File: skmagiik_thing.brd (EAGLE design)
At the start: 160 x 100 mm, 24 parts, among them J1 MAGJACK-NOLABELS, U1 AUDIO-JACK, U2 AUDIO-JACK, U3 MAX3232

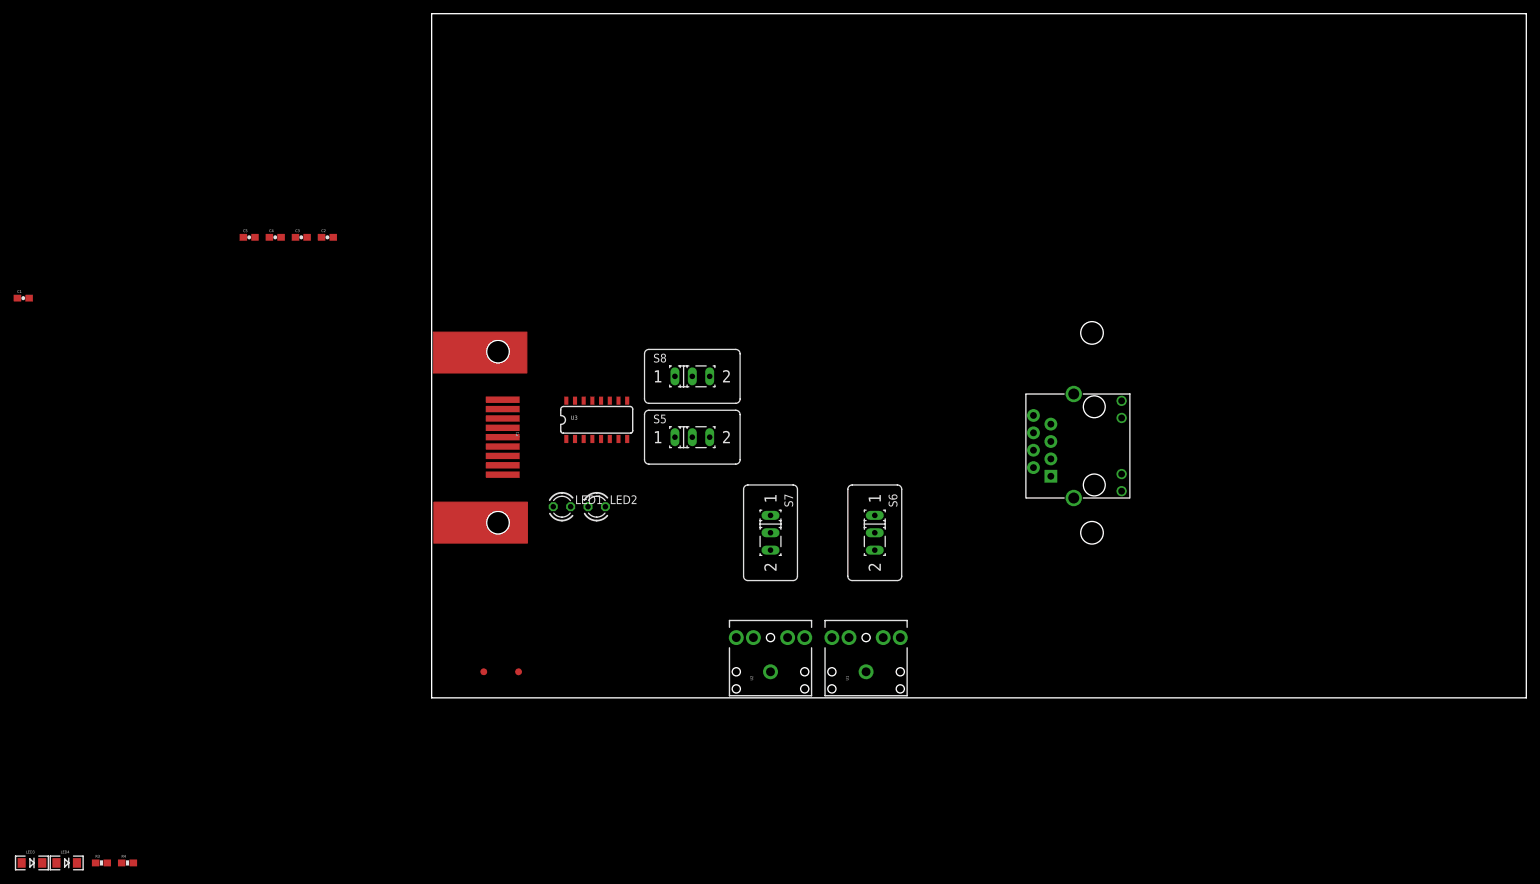
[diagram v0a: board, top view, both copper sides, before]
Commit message: changed to use modules, added pdf of layout
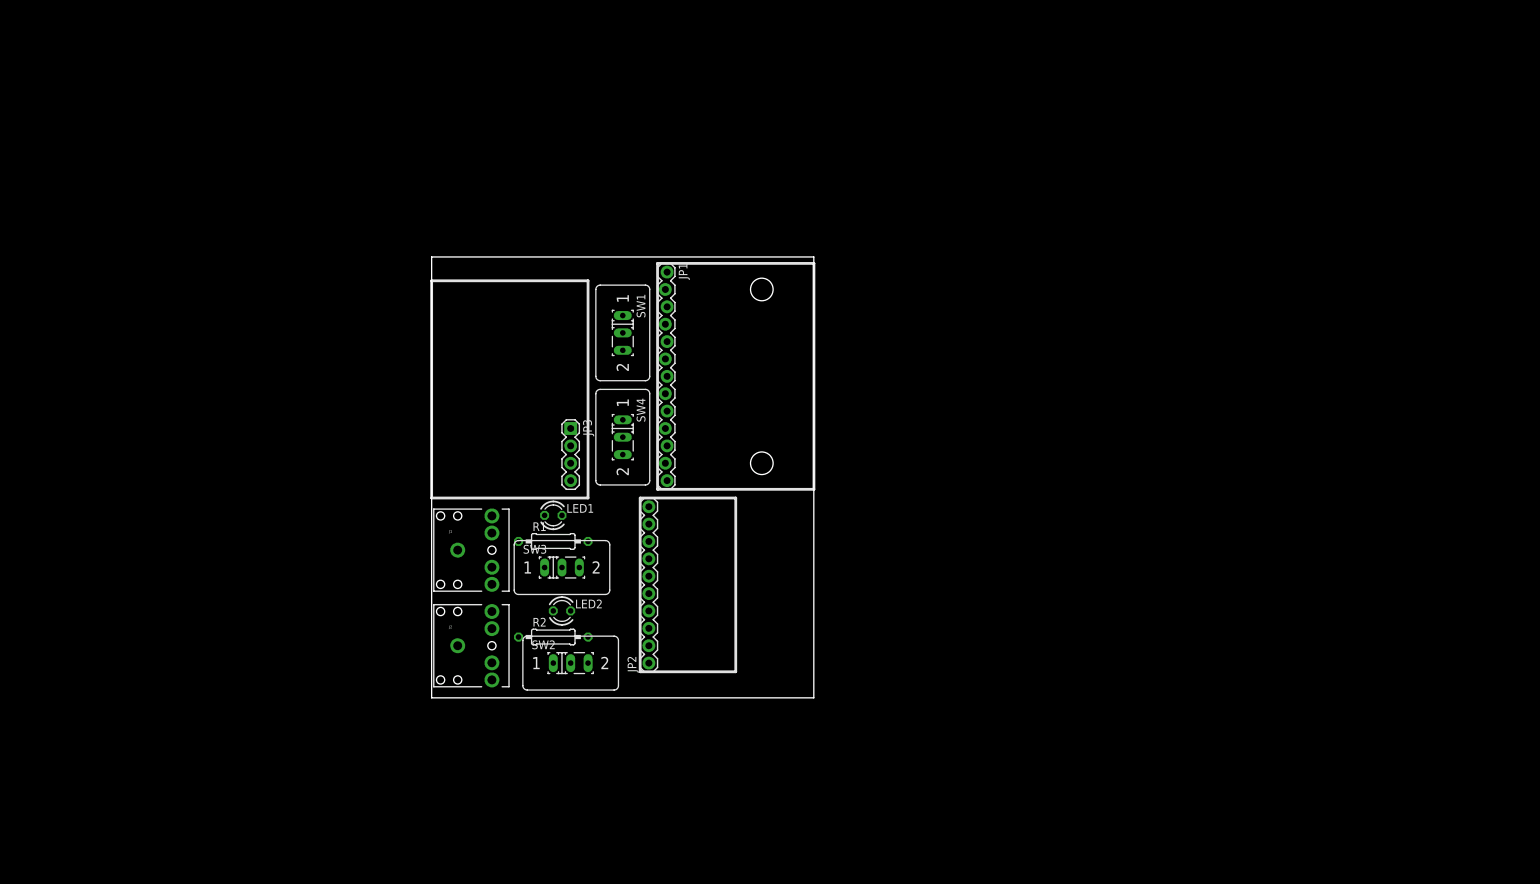
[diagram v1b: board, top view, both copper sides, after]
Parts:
- removed C1, C2, C3, C4, C5: .1uF, SparkFun-Capacitors:0603-CAP
- removed FID1, FID2: FIDUCIAL1X2, SparkFun-Aesthetics:FIDUCIAL-1X2
- removed LED3: Red, SparkFun:LED-1206
- removed LED4: Grn, SparkFun:LED-1206
- removed R3, R4: 330, SparkFun:0603-RES
- removed S5, S6, S7, S8: (no value), switch:M251
- removed U1, U2: AUDIO-JACK, SparkFun:AUDIO-JACK
- removed U3: MAX3232, SparkFun-DigitalIC:SO016
- added J2: AUDIO-JACK, SparkFun:AUDIO-JACK
- added JP2: M10", SparkFun-Connectors:1X10
- added JP3: (no value), SparkFun:1X04
- added R1, R2: (no value), resistor:0207/10
- added SW1, SW2, SW3, SW4: (no value), switch:M251
- J1: value MAGJACK-NOLABELS -> AUDIO-JACK; device SparkFun-Connectors:MAGJACK -> SparkFun:AUDIO-JACK
- JP1: value DB9 -> M13LOCK; device Testing:DB9-L17SM209S114T -> SparkFun-Connectors:1X13_LOCK
- moved J1 104.4 mm to (3.81, 21.6), turned to 0 degrees
- moved STANDOFF3 49.3 mm to (48.3, 34.3)
- moved STANDOFF5 48.7 mm to (48.3, 59.7)
- moved JP1 36.9 mm to (34.3, 62.2), turned to 270 degrees
- moved LED2 16.1 mm to (19.1, 12.7)
- moved LED1 1.80 mm to (17.8, 26.7)
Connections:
- removed net C1+: C1.1, U3.1
- removed net C1-: C1.2, U3.3
- removed net C2+: C2.1, U3.4
- removed net C2-: C2.2, U3.5
- removed net N$15: S8.3, U3.8
- removed net N$16: S7.3, U3.7
- removed net V+: C3.1, U3.2
- removed net V-: C4.1, U3.6
- net GND: now also J1.SLEEVE, J2.SLEEVE, JP1.9, JP2.6, JP3.2; no longer C3.2, C4.2, C5.2, J1.5, JP1.5, U1.SLEEVE, U2.SLEEVE, U3.15
- net N$1: now also J2.RING, R2.1; no longer LED2.K, U2.RING
- net N$10: now also JP2.1, SW2.3; no longer LED4.A, R4.1
- net N$11: now also JP2.9, JP3.4, SW1.1; no longer JP1.3, U3.13
- net N$12: now also LED1.K, R1.2; no longer JP1.2, U3.14
- net N$13: now also JP2.3, SW1.3; no longer LED4.C, S8.1, U3.11, U3.9
- net N$14: now also LED2.K, R2.2; no longer LED3.C, S7.1, U3.10, U3.12
- net N$17: now also JP1.12, SW1.2; no longer J1.2, S8.2
- net N$18: now also JP1.11, SW2.2; no longer J1.3, S7.2
- net N$2: now also J1.RING, R1.1; no longer LED1.K, U1.RING
- net N$3: now also JP1.7, SW4.1; no longer J1.7, S6.1
- net N$4: now also JP1.8, SW4.3; no longer J1.6, S6.3
- net N$5: now also JP1.10, SW3.3; no longer J1.4, S5.3
- net N$6: now also JP1.13, SW3.1; no longer J1.1, S5.1
- net N$7: now also SW4.2; no longer S6.2
- net N$8: now also SW3.2; no longer S5.2
- net N$9: now also JP2.7, JP3.3, SW2.1; no longer LED3.A, R3.1
- net VCC: now also J1.TIP, J2.TIP, JP1.6, JP2.5, JP3.1; no longer C5.1, J1.8, R3.2, R4.2, U1.TIP, U2.TIP, U3.16
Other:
- board size 160 x 100 mm -> 55.9 x 64.4 mm

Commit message: modifyed layout
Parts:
- moved SW4 34.2 mm to (19.1, 5.08), turned to 0 degrees
- moved SW2 33.9 mm to (27.9, 38.1), turned to 270 degrees
- moved JP2 32.2 mm to (36.8, 36.8)
- moved STANDOFF3 30.5 mm to (48.3, 3.81)
- moved JP1 30.5 mm to (34.3, 31.8)
- moved STANDOFF5 30.5 mm to (48.3, 29.2)
- moved R1 10.2 mm to (27.9, 21.6), turned to 270 degrees
- moved R2 10.2 mm to (27.9, 7.62), turned to 270 degrees
- moved LED1 1.80 mm to (19.1, 25.4)
- moved LED2 1.27 mm to (19.1, 11.4)
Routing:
- net N$2: track 0.00 -> 20.2 mm
- net N$1: track 0.00 -> 20.2 mm
- net VCC: track 0.00 -> 15.5 mm
- net N$14: track 0.00 -> 15.4 mm
- net N$12: track 0.00 -> 15.4 mm
- net GND: track 0.00 -> 15.0 mm
- net N$7: track 0.00 -> 6.88 mm
- net N$8: track 0.00 -> 6.88 mm

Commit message: layour ready for aproval
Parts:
- removed JP1: M13LOCK, SparkFun-Connectors:1X13_LOCK
- added J3: RJ45, pjb:RJ45
- moved STANDOFF3 6.35 mm to (41.9, 3.81)
- moved STANDOFF5 6.35 mm to (41.9, 29.2)
- moved JP2 1.91 mm to (34.9, 36.8)
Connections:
- net GND: now also J3.5; no longer JP1.9
- net N$17: now also J3.2; no longer JP1.12
- net N$18: now also J3.3; no longer JP1.11
- net N$3: now also J3.7; no longer JP1.7
- net N$4: now also J3.6; no longer JP1.8
- net N$5: now also J3.4; no longer JP1.10
- net N$6: now also J3.1; no longer JP1.13
- net VCC: now also J3.8; no longer JP1.6
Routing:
- net GND: track 15.0 -> 105.0 mm, vias 0 -> 2
- net VCC: track 15.5 -> 95.2 mm
- net N$17: track 0.00 -> 47.9 mm, vias 0 -> 1
- net N$4: track 0.00 -> 45.2 mm
- net N$3: track 0.00 -> 43.9 mm
- net N$9: track 0.00 -> 41.4 mm
- net N$11: track 0.00 -> 37.4 mm
- net N$18: track 0.00 -> 32.0 mm
- net N$6: track 0.00 -> 23.8 mm
- net N$5: track 0.00 -> 14.4 mm
- net N$13: track 0.00 -> 14.4 mm, vias 0 -> 1
- net N$10: track 0.00 -> 7.51 mm
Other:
- board size 55.9 x 64.4 mm -> 47.6 x 61.3 mm

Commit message: exported gerbers
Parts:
- added U$2: PROJECT_LOGO, links_misc:BMP_TEST
- moved STANDOFF3 1.27 mm to (40.6, 3.81)
- moved STANDOFF5 1.27 mm to (40.6, 29.2)
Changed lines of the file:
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@@
 <element name="SW2" library="switch" package="M251" value="" x="27.94" y="38.1" rot="R270"/>
 <element name="SW1" library="switch" package="M251" value="" x="27.94" y="53.34" rot="R270"/>
-<element name="STANDOFF3" library="SparkFun-Electromechanical" package="STAND-OFF" value="STAND-OFF" x="41.91" y="3.81"/>
-<element name="STANDOFF5" library="SparkFun-Electromechanical" package="STAND-OFF" value="STAND-OFF" x="41.91" y="29.21"/>
+<element name="STANDOFF3" library="SparkFun-Electromechanical" package="STAND-OFF" value="STAND-OFF" x="40.64" y="3.81"/>
+<element name="STANDOFF5" library="SparkFun-Electromechanical" package="STAND-OFF" value="STAND-OFF" x="40.64" y="29.21"/>
 <element name="JP2" library="SparkFun-Connectors" package="1X10" value="M10&quot;" x="34.925" y="36.83" rot="R90">
 <attribute name="NO_PART" value="1" x="34.925" y="36.83" size="1.778" layer="27" rot="R90" display="off"/>
@@
 <element name="R2" library="resistor" package="0207/10" value="" x="27.94" y="7.62" rot="R270"/>
 <element name="J3" library="pjb" package="RJ45" value="RJ45" x="41.91" y="16.51" rot="R270"/>
+<element name="U$2" library="links_misc" package="BMP_TEST" value="PROJECT_LOGO" x="32.385" y="27.94"/>
 </elements>
 <signals>
